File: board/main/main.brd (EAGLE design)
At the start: 108.5 x 39 mm, 38 parts, among them IC1 78m05, J1 188275-8, U1 6N138M, U2 MMBD4148TW-7-F, U3 MMBD4148TW-7-F, U4 MMBD4148TW-7-F

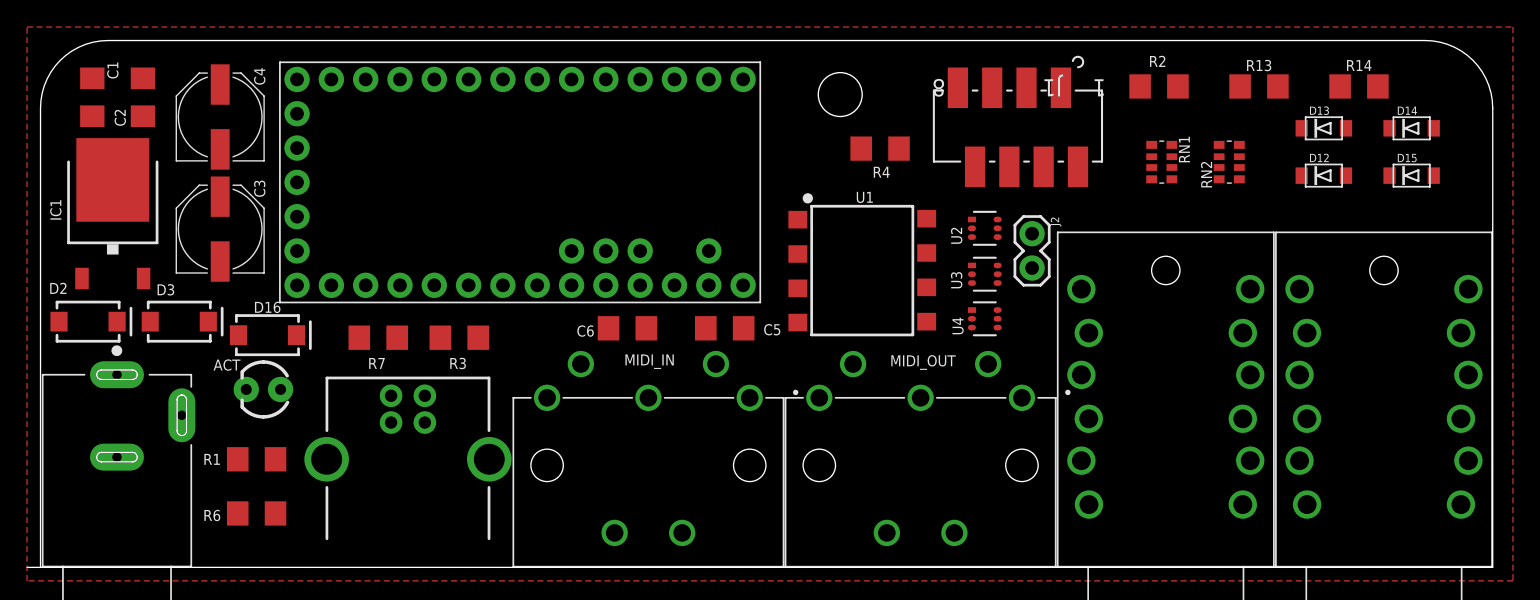
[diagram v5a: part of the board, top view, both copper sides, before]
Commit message: submitted REV C of the main board for manufacture
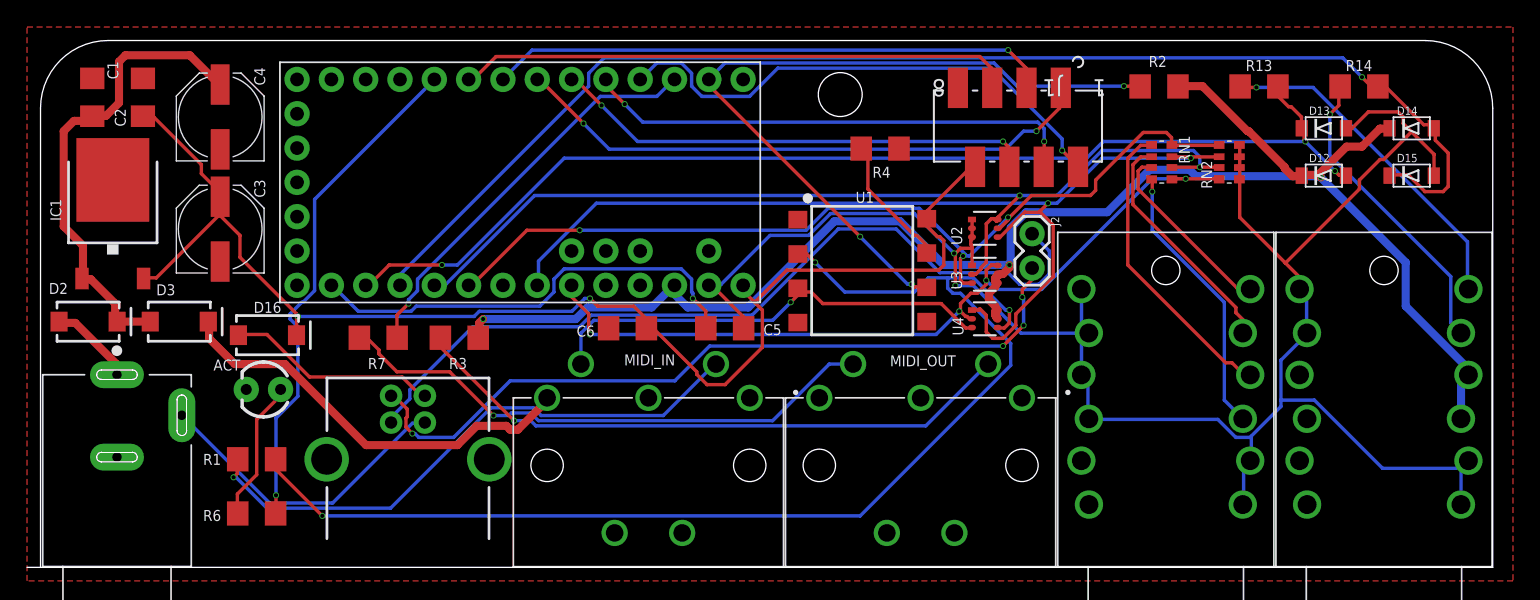
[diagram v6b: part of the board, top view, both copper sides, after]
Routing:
- net AGND: track 0.00 -> 142.5 mm, vias 0 -> 2
- net 3V: track 0.00 -> 122.6 mm, vias 0 -> 3
- net VIN: track 0.00 -> 99.6 mm, vias 0 -> 2
- net JACK2: track 0.00 -> 96.5 mm, vias 0 -> 1
- net SIG-C: track 0.00 -> 90.2 mm, vias 0 -> 3
- net JACK1: track 0.00 -> 83.1 mm, vias 0 -> 3
- net JACK5: track 0.00 -> 77.0 mm, vias 0 -> 2
- net JACK3: track 0.00 -> 73.4 mm, vias 0 -> 2
- net JACK4: track 0.00 -> 68.8 mm, vias 0 -> 3
- net N$10: track 0.00 -> 60.8 mm
- net JACK6: track 0.00 -> 60.5 mm, vias 0 -> 4
- net N$13: track 0.00 -> 57.1 mm, vias 0 -> 4
- net RX: track 0.00 -> 55.9 mm, vias 0 -> 3
- net N$6: track 0.00 -> 45.5 mm, vias 0 -> 1
- net FS1_LED: track 0.00 -> 43.7 mm, vias 0 -> 2
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
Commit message: board changes
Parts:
- added R5, R8: 100, SparkFun-Resistors:1206
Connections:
- new net N$14: EXP.11, R5.1
- new net N$19: EXP.5, R8.1
- net 3V: now also R5.2, R8.2; no longer EXP.11, EXP.5
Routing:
- net 3V: track 122.6 -> 99.7 mm
- net N$19: track 0.00 -> 19.3 mm
- net SIG-C: track 90.2 -> 72.6 mm
- net N$14: track 0.00 -> 13.6 mm
- net VIN: track 99.6 -> 90.3 mm, vias 2 -> 3
- net TX: track 30.1 -> 37.1 mm
- net JACK2: track 96.5 -> 103.2 mm
- net FS2_LED: track 41.7 -> 46.7 mm
- net JACK5: track 77.0 -> 72.3 mm
- net JACK3: track 73.4 -> 77.4 mm
- net JACK6: track 60.5 -> 63.9 mm, vias 4 -> 1
- net AGND: track 142.5 -> 139.8 mm
- net N$13: track 57.1 -> 54.5 mm, vias 4 -> 3
- net FS2: track 37.1 -> 39.5 mm, vias 2 -> 1
- net FS1_LED: track 43.7 -> 41.9 mm, vias 2 -> 1
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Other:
- board text added: "11/03/2020 REV: D"
- board text removed: "?/?/202? REV: C"

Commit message: Main board, revision E
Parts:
- removed D12, D13, D14, D15: SM5817, adafruit:SOD-123FL
- removed R13, R14, R2: 1K, SparkFun-Resistors:1206
- added RN3: 1K, resistor-dil:EXB38V
- added U5: BAT54SDW-7-F, BAT54SDW7F:SOT-363_DIO
- moved R7 61.6 mm to (86.6, 15.0)
- moved R1 60.3 mm to (75.4, 18.2)
- moved R3 55.8 mm to (86.6, 12.0)
- moved U2 28.7 mm to (97.6, 32.6), turned to 270 degrees
- moved U3 28.2 mm to (97.6, 27.0), turned to 270 degrees
- moved R4 27.3 mm to (87.2, 20.0), turned to 270 degrees
- moved U4 25.7 mm to (92.9, 29.9), turned to 270 degrees
- moved C6 24.9 mm to (68.2, 20.2), turned to 270 degrees
- moved U1 24.6 mm to (84.6, 28.7)
- moved RN1 20.0 mm to (102.9, 28.2), turned to 0 degrees
- moved C2 17.0 mm to (16.4, 20.2), turned to 270 degrees
- moved TRIG1 15.1 mm to (98.4, 8.30)
- moved EXP 15.1 mm to (114.5, 8.30)
- moved RN2 14.9 mm to (102.9, 31.0), turned to 180 degrees
- moved C1 13.7 mm to (16.4, 29.4)
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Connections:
- net 3V: now also RN3.3, U5.2, U5.5; no longer D12.C, D14.C, R2.1
- net AGND: now also U5.1, U5.4; no longer D13.A, D15.A
- net JACK1: now also RN3.8, U5.6; no longer D12.A, D13.C, R13.2
- net JACK2: now also RN3.7, U5.3; no longer D14.A, D15.C, R14.2
- net N$18: now also RN3.1; no longer R13.1
- net N$21: now also RN3.2; no longer R14.1
- net RX: now also RN3.6; no longer R2.2
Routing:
- net AGND: track 139.8 -> 187.0 mm, vias 2 -> 3
- net JACK1: track 84.0 -> 129.4 mm, vias 4 -> 3
- net SIG-C: track 72.6 -> 27.6 mm, vias 3 -> 0
- net N$6: track 45.5 -> 8.81 mm, vias 1 -> 0
- net JACK6: track 63.9 -> 97.3 mm, vias 1 -> 4
- net SIG-A: track 34.7 -> 64.2 mm, vias 1 -> 3
- net N$3: track 42.5 -> 17.8 mm, vias 1 -> 0
- net N$4: track 33.7 -> 9.46 mm, vias 1 -> 0
- net N$8: track 41.2 -> 18.9 mm, vias 1 -> 0
- net N$5: track 31.3 -> 51.3 mm, vias 0 -> 1
- net N$13: track 54.5 -> 74.3 mm, vias 3 -> 0
- net JACK4: track 69.3 -> 88.5 mm, vias 3 -> 6
- net RX: track 56.6 -> 72.3 mm
- net N$18: track 26.2 -> 10.9 mm, vias 1 -> 0
- net ACT_LED: track 37.5 -> 23.4 mm
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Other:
- board size 108.5 x 39 mm -> 123.6 x 35.4 mm
- board text added: "11/15/2020 REV: E"
- board text removed: "11/03/2020 REV: D"
